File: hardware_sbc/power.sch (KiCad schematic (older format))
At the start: 59 parts, among them J6 Conn_01x02, J7 S2B-PH-K-S(LF)(SN), J8 Conn_01x01_Male, J9 0874380343, Q1 Q_NMOS_GSD, U10 MIC94164, U11 BQ29702, U12 BQ27426, U5 MP2636GR-P, U6 NCP133AMX150TCG

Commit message: Correct U12 BIN pin connection
Fixes #5
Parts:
- removed Q1: Q_NMOS_GSD, Package_DFN_QFN:Diodes_DFN1006-3, symbol Device:Q_NMOS_GSD
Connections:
- wire segments 215 -> 212
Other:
- moved on the sheet: R51
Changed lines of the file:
@@
 Wire Wire Line
 	6050 7150 6350 7150
-$Comp
-L Device:Q_NMOS_GSD Q1
-U 1 1 5EB42DA8
-P 3400 9750
-F 0 "Q1" H 3604 9796 50  0000 L CNN
-F 1 "Q_NMOS_GSD" H 3604 9705 50  0000 L CNN
-F 2 "Package_DFN_QFN:Diodes_DFN1006-3" H 3600 9850 50  0001 C CNN
-F 3 "~" H 3400 9750 50  0001 C CNN
-F 4 "1727-2231-1-ND" H 3605 9659 50  0001 L CNN "Vendorpart"
-F 5 "NXP" H 3400 9750 50  0001 C CNN "Mfgr"
-F 6 "" H 3400 9750 50  0001 C CNN "Part"
-F 7 "NX7002BKMB" H 3400 9750 50  0001 C CNN "Mfgrpart"
-	1    3400 9750
-	1    0    0    -1
-$EndComp
-$Comp
-L Device:R R?
-U 1 1 5EB4705F
-P 3500 9200
-AR Path="/5EB4705F" Ref="R?"  Part="1"
-AR Path="/5DC6F4F1/5EB4705F" Ref="R51"  Part="1"
-F 0 "R51" H 3431 9154 50  0000 R CNN
-F 1 "10K" H 3431 9245 50  0000 R CNN
-F 2 "Resistor_SMD:R_0201_0603Metric" V 3430 9200 50  0001 C CNN
-F 3 "~" H 3500 9200 50  0001 C CNN
-F 4 "Panasonic" H 3500 9200 50  0001 C CNN "Mfgr"
-F 5 "" H 3500 9200 50  0001 C CNN "Part"
-F 6 "P123222CT-ND" H 3500 9200 50  0001 C CNN "Vendorpart"
-F 7 "ERJ-1GNJ103C" H 3500 9200 50  0001 C CNN "Mfgrpart"
-	1    3500 9200
-	1    0    0    1
-$EndComp
-Wire Wire Line
-	3500 9350 3500 9500
 Wire Wire Line
 	4300 9150 4100 9150
 Wire Wire Line
 	4100 9150 4100 9500
-Wire Wire Line
-	4100 9500 3500 9500
-Connection ~ 3500 9500
-Wire Wire Line
-	3500 9500 3500 9550
-$Comp
-L power:GND #PWR0233
-U 1 1 5EB7DFBB
-P 3500 9950
-F 0 "#PWR0233" H 3500 9700 50  0001 C CNN
-F 1 "GND" H 3505 9777 50  0000 C CNN
-F 2 "" H 3500 9950 50  0001 C CNN
-F 3 "" H 3500 9950 50  0001 C CNN
-	1    3500 9950
-	1    0    0    -1
-$EndComp
-Text Label 3100 9750 2    50   ~ 0
-DCHG_EN
-Wire Wire Line
-	3100 9750 3200 9750
 $Comp
 L Device:C C141
@@
 Wire Wire Line
 	6150 9350 6150 8950
-Text Label 4100 9500 0    50   ~ 0
-BIN
 Text Label 4100 9000 0    50   ~ 0
 GPOUT
@@
 Text Notes 4500 9400 0    50   ~ 0
 7-bit addr: 0x55
-Text Label 3500 8950 2    50   ~ 0
-BQ_VDD
-Wire Wire Line
-	3500 8950 3500 9050
 $Comp
 L mxenc:VDD_1V8 #PWR?
@@
 Text Notes 5800 4300 1    50   ~ 0
 Ttotal_tmr =\n4.9 Hr @1A
+Text Label 4100 9500 0    50   ~ 0
+BIN
+$Comp
+L Device:R R?
+U 1 1 5EB4705F
+P 3850 9750
+AR Path="/5EB4705F" Ref="R?"  Part="1"
+AR Path="/5DC6F4F1/5EB4705F" Ref="R51"  Part="1"
+F 0 "R51" H 3781 9704 50  0000 R CNN
+F 1 "10K" H 3781 9795 50  0000 R CNN
+F 2 "Resistor_SMD:R_0201_0603Metric" V 3780 9750 50  0001 C CNN
+F 3 "~" H 3850 9750 50  0001 C CNN
+F 4 "Panasonic" H 3850 9750 50  0001 C CNN "Mfgr"
+F 5 "" H 3850 9750 50  0001 C CNN "Part"
+F 6 "P123222CT-ND" H 3850 9750 50  0001 C CNN "Vendorpart"
+F 7 "ERJ-1GNJ103C" H 3850 9750 50  0001 C CNN "Mfgrpart"
+	1    3850 9750
+	1    0    0    1
+$EndComp
+Wire Wire Line
+	4100 9500 3850 9500
+Wire Wire Line
+	3850 9500 3850 9600
+$Comp
+L power:GND #PWR?
+U 1 1 5F40E553
+P 3850 9900
+F 0 "#PWR?" H 3850 9650 50  0001 C CNN
+F 1 "GND" H 3855 9727 50  0000 C CNN
+F 2 "" H 3850 9900 50  0001 C CNN
+F 3 "" H 3850 9900 50  0001 C CNN
+	1    3850 9900
+	1    0    0    -1
+$EndComp
 $EndSCHEMATC

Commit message: Add low-side FET to properly disconnect battery on fault
What was done in v0.9 to disable charge/discharge by driving IO on
the charger circuit didn't really work out. Further, it had no way
of monitoring overcurrent during discharge.

Add a FED on the low side of the pack that can be controlled by the
protection circuit, since this is how it is supposed to work.

Fixes #6
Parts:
- added R71, R72: 5M, Resistor_SMD:R_0201_0603Metric, symbol Device:R
- added U14: CSD85302L, mxenc:CSD85302L, symbol mxenc:CSD85302L
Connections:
- net CHG_EN: no longer U11.2 (COUT)
- net DCHG_EN: no longer U11.3 (DOUT)
- net GND: now also R71.1, U14.4 (S1); no longer J7.2 (Pin_2), J9.3 (Pin_3)
- new net COUT: R72.2, U11.2 (COUT), U14.3 (G2)
- new net DOUT: R71.2, U11.3 (DOUT), U14.1 (G1)
- new net GND1: J7.2 (Pin_2), J9.3 (Pin_3), R72.1, U14.2 (S2)
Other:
- moved on the sheet: C141, C148, R51, R54, U12

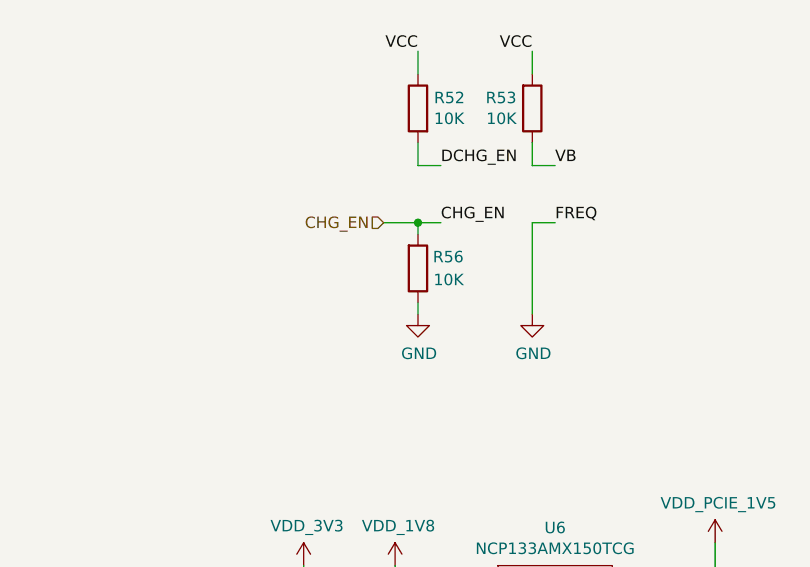
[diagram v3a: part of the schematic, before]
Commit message: Enable charging by default, remove processor control
Having the charge enable hooked up to the processor was problematic
when the pin is not configured. There's not a great case for needing
to have the processor enable/disable charging, so just leave it
enabled.
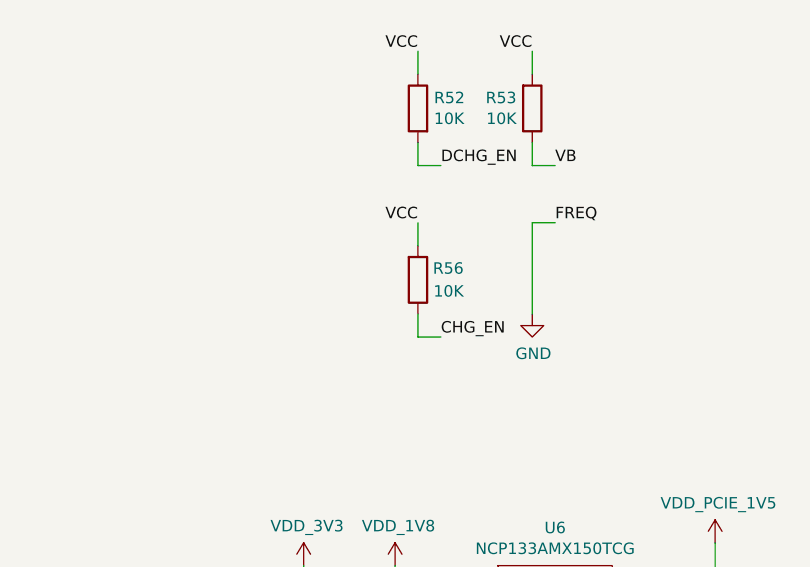
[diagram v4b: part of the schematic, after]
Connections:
- net CHG_EN: now also R56.1; no longer R56.2
- net GND: no longer R56.1
- net VCC: now also R56.2
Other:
- moved on the sheet: R56
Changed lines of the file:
@@
 Wire Wire Line
 	3050 4250 3150 4250
-Connection ~ 3050 4500
-Wire Wire Line
-	2900 4500 3050 4500
-Text HLabel 2900 4500 0    50   Input ~ 0
-CHG_EN
-Wire Wire Line
-	3050 4550 3050 4500
-Wire Wire Line
-	3050 4900 3050 4850
-$Comp
-L power:GND #PWR0158
-U 1 1 5EC68829
-P 3050 4900
-F 0 "#PWR0158" H 3050 4650 50  0001 C CNN
-F 1 "GND" H 3055 4727 50  0000 C CNN
-F 2 "" H 3050 4900 50  0001 C CNN
-F 3 "" H 3050 4900 50  0001 C CNN
-	1    3050 4900
-	1    0    0    -1
-$EndComp
 Wire Wire Line
 	3550 4500 3550 4900
 Wire Wire Line
 	3650 4500 3550 4500
-Text Label 3150 4500 0    50   ~ 0
+Text Label 3150 5000 0    50   ~ 0
 CHG_EN
 Text Label 3650 4500 0    50   ~ 0
@@
 $EndComp
 Wire Wire Line
-	3150 4500 3050 4500
+	3150 5000 3050 5000
 $Comp
 L Device:R R?
 U 1 1 5EA46BAD
-P 3050 4700
+P 3050 4750
 AR Path="/5EA46BAD" Ref="R?"  Part="1"
 AR Path="/5DC6F4F1/5EA46BAD" Ref="R56"  Part="1"
-F 0 "R56" H 3250 4650 50  0000 R CNN
-F 1 "10K" H 3250 4750 50  0000 R CNN
-F 2 "Resistor_SMD:R_0201_0603Metric" V 2980 4700 50  0001 C CNN
-F 3 "~" H 3050 4700 50  0001 C CNN
-F 4 "Panasonic" H 3050 4700 50  0001 C CNN "Mfgr"
-F 5 "" H 3050 4700 50  0001 C CNN "Part"
-F 6 "P123222CT-ND" H 3050 4700 50  0001 C CNN "Vendorpart"
-F 7 "ERJ-1GNJ103C" H 3050 4700 50  0001 C CNN "Mfgrpart"
-	1    3050 4700
+F 0 "R56" H 3250 4700 50  0000 R CNN
+F 1 "10K" H 3250 4800 50  0000 R CNN
+F 2 "Resistor_SMD:R_0201_0603Metric" V 2980 4750 50  0001 C CNN
+F 3 "~" H 3050 4750 50  0001 C CNN
+F 4 "Panasonic" H 3050 4750 50  0001 C CNN "Mfgr"
+F 5 "" H 3050 4750 50  0001 C CNN "Part"
+F 6 "P123222CT-ND" H 3050 4750 50  0001 C CNN "Vendorpart"
+F 7 "ERJ-1GNJ103C" H 3050 4750 50  0001 C CNN "Mfgrpart"
+	1    3050 4750
 	1    0    0    1
 $EndComp
@@
 Wire Wire Line
 	6200 8750 6250 8750
+Wire Wire Line
+	3050 4900 3050 5000
+Text Label 3050 4500 2    50   ~ 0
+VCC
+Wire Wire Line
+	3050 4500 3050 4600
 $EndSCHEMATC

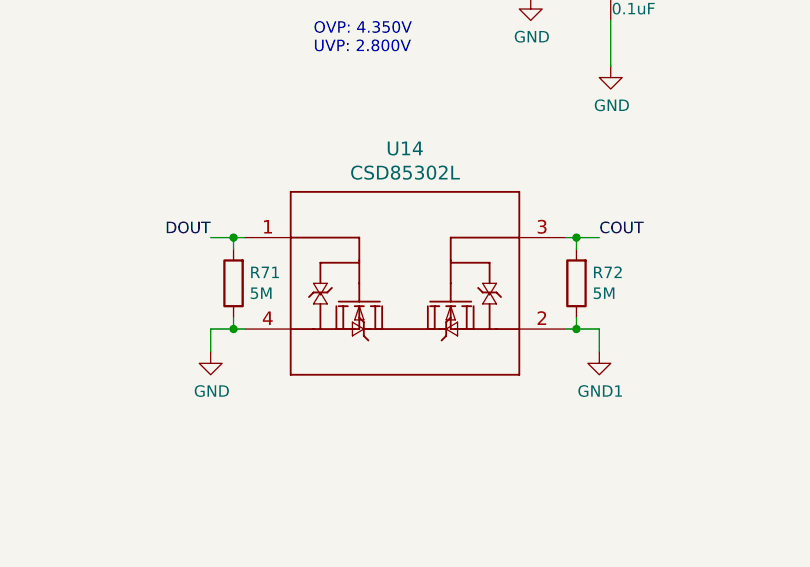
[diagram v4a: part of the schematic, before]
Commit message: Fill in missing part numbers for bom
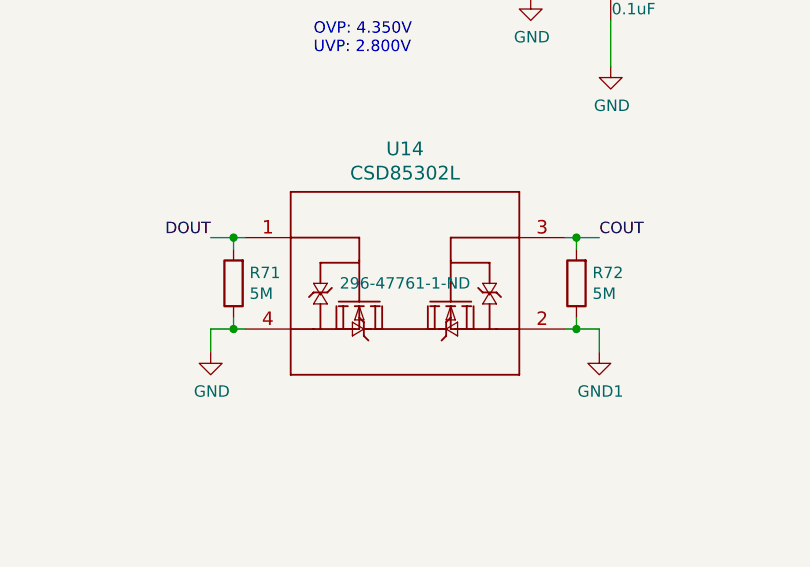
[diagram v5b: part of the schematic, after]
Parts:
- U14: Mfgr (none) -> TI; Mfgrpart (none) -> CSD85302L; Vendorpart (none) -> 296-47761-1-ND
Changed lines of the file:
@@
 F 2 "mxenc:CSD85302L" H 6950 8490 60  0001 C CNN
 F 3 "" H 6950 8550 60  0000 C CNN
+F 4 "296-47761-1-ND" H 6950 8550 50  0000 C CNN "Vendorpart"
+F 5 "TI" H 6950 8550 50  0001 C CNN "Mfgr"
+F 6 "CSD85302L" H 6950 8550 50  0001 C CNN "Mfgrpart"
 	1    6950 8550
 	1    0    0    1
